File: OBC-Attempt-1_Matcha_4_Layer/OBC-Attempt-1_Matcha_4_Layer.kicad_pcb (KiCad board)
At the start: 4 copper layers, 75 parts, among them J1 Screw_Terminal_01x08, J2 Screw_Terminal_01x08, J3 USB_B_Micro, J4 Screw_Terminal_01x08, J5 Conn_01x04, J6 Micro_SD_Card, J7 Screw_Terminal_01x02, J8 Screw_Terminal_01x02, Q1 2N7002K, Q2 2N7002K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

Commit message: Some 4 Layer Work :)
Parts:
- removed C14: 26pf, Capacitor_SMD:C_01005_0402Metric
- removed C18: 26uf, Capacitor_SMD:C_01005_0402Metric
- removed Y2: ABMM2-32.768MHZ-E2F-T, ABMM2_6mm_3_6mm:XTAL_ABMM2-32.768MHZ-E2F-T
- added H1: MountingHole_Pad, MountingHole:MountingHole_3mm_Pad_TopBottom, F.Cu at (76.2, 31.8)
- added H2: MountingHole_Pad, MountingHole:MountingHole_3mm_Pad_TopBottom, F.Cu at (31.8, 31.8)
- added H3: MountingHole_Pad, MountingHole:MountingHole_3mm_Pad_TopBottom, F.Cu at (31.8, 76.2)
- added H4: MountingHole_Pad, MountingHole:MountingHole_3mm_Pad_TopBottom, F.Cu at (76.2, 76.2)
- BZ1, J5, Q1, Q2, Q3, Q4, R10, R11, R12, R14, R15, R16, R17, R9, U10, U11, U2, U3, U4, U5, U7, U8: moved to B.Cu
- C1, C10, C11, C13, C15, C16, C17, C2, C3, C4, C6, C7, C8, C9: footprint Capacitor_SMD:C_01005_0402Metric -> Capacitor_SMD:C_0402_1005Metric
- C12, C5: footprint Capacitor_SMD:C_0201_0603Metric -> Capacitor_SMD:C_0603_1608Metric; moved to F.Cu
- C20, C21: footprint Capacitor_SMD:C_0201_0603Metric -> Capacitor_SMD:C_0603_1608Metric
- D1, D2, D3, D4, D5, D6, D7, D8: footprint Diode_SMD:D_SMC -> Diode_SMD:D_SMA; moved to B.Cu
- J1, J2, J4: footprint TerminalBlock_Phoenix:TerminalBlock_Phoenix_MKDS-1,5-8_1x08_P5.00mm_Horizontal -> TerminalBlock_Phoenix:TerminalBlock_Phoenix_MPT-0,5-8-2.54_1x08_P2.54mm_Horizontal
- J3, U6: moved to F.Cu
- J7, J8: footprint TerminalBlock_Phoenix:TerminalBlock_Phoenix_MKDS-1,5-2_1x02_P5.00mm_Horizontal -> TerminalBlock_Phoenix:TerminalBlock_Phoenix_MPT-0,5-2-2.54_1x02_P2.54mm_Horizontal; moved to B.Cu
- R1, R2, R3, R4, R5, R6, R7, R8: footprint Resistor_SMD:R_0201_0603Metric -> Resistor_SMD:R_0603_1608Metric; moved to B.Cu
- R13: footprint Resistor_SMD:R_01005_0402Metric -> Resistor_SMD:R_0603_1608Metric
- R18, R19: footprint Resistor_SMD:R_0201_0603Metric -> Resistor_SMD:R_0603_1608Metric
- moved J3 139.4 mm to (40.7, 28.3), turned to 180 degrees
- moved J7 135.2 mm to (40.5, 78.8)
- moved J8 133.2 mm to (47.4, 78.8), turned to 180 degrees
- moved C5 131.9 mm to (42.8, 32.0)
- moved C12 125.3 mm to (46.1, 42.6), turned to 0 degrees
- moved R18 124.0 mm to (50.0, 72.5), turned to 90 degrees
- moved C20 123.5 mm to (48.0, 72.5), turned to 90 degrees
- moved U6 122.9 mm to (44.0, 37.3), turned to -90 degrees
- moved U12 120.7 mm to (43.5, 70.6), turned to 90 degrees
- moved R19 120.3 mm to (50.0, 69.4), turned to 90 degrees
- moved C21 112.2 mm to (44.6, 63.2), turned to 180 degrees
- moved J6 106.0 mm to (63.7, 74.0), turned to 0 degrees
- moved U1 94.2 mm to (55.7, 51.5), turned to 135 degrees
- moved C7 89.1 mm to (55.8, 45.9), turned to 180 degrees
- moved C9 88.8 mm to (57.2, 46.8), turned to 90 degrees
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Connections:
- C20 pad 1: PWR -> BATT+
- R18 pad 1: PWR -> unconnected-(R18-Pad1)
- U12 pad 3: PWR -> BATT+
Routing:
- net GND: track 174.6 -> 0.00 mm, vias 5 -> 0
- net PWR: track 87.8 -> 0.00 mm
- net 3.3V: track 39.3 -> 0.00 mm, vias 4 -> 0
- net USB_OTG_FS_ID: track 35.0 -> 0.00 mm, vias 1 -> 0
- net SDIO_CMD: track 34.0 -> 0.00 mm
- net VMON: track 33.4 -> 0.00 mm
- net USB_OTG_FS_DP: track 32.4 -> 0.00 mm, vias 1 -> 0
- net SDIO_D3: track 30.3 -> 0.00 mm
- net SDIO_D0: track 29.8 -> 0.00 mm
- net SDIO_CK: track 26.7 -> 0.00 mm
- net USB_OTG_FS_DM: track 25.7 -> 0.00 mm, vias 1 -> 0
- net SDIO_D1: track 25.6 -> 0.00 mm
- net SDIO_D2: track 24.2 -> 0.00 mm
- net BATT+: track 17.3 -> 0.00 mm
- net RCC_OSC_IN: track 11.9 -> 0.00 mm
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- added copper zone on In2.Cu, net 3.3V
- added copper zone on In1.Cu, net GND
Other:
- board outline added: 57.1 x 57.1 mm

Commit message: start over
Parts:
- moved C5 175.9 mm to (200.2, 110.4)
- moved C12 175.9 mm to (203.6, 121.0)
- moved J3 175.9 mm to (198.2, 106.7)
- moved U6 175.9 mm to (201.4, 115.7)
- moved D4 158.3 mm to (189.0, 25.9)
- moved R11 158.3 mm to (199.9, 38.0)
- moved R9 158.3 mm to (199.7, 31.0)
- moved U4 158.3 mm to (194.6, 39.3)
- moved D1 158.3 mm to (189.0, 40.1)
- moved D2 158.3 mm to (189.0, 18.7)
- moved D3 158.3 mm to (189.0, 33.0)
- moved J2 158.3 mm to (185.6, 38.7)
- moved R10 158.3 mm to (199.7, 23.9)
- moved R12 158.3 mm to (199.6, 16.7)
- moved U2 158.3 mm to (194.4, 32.3)
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
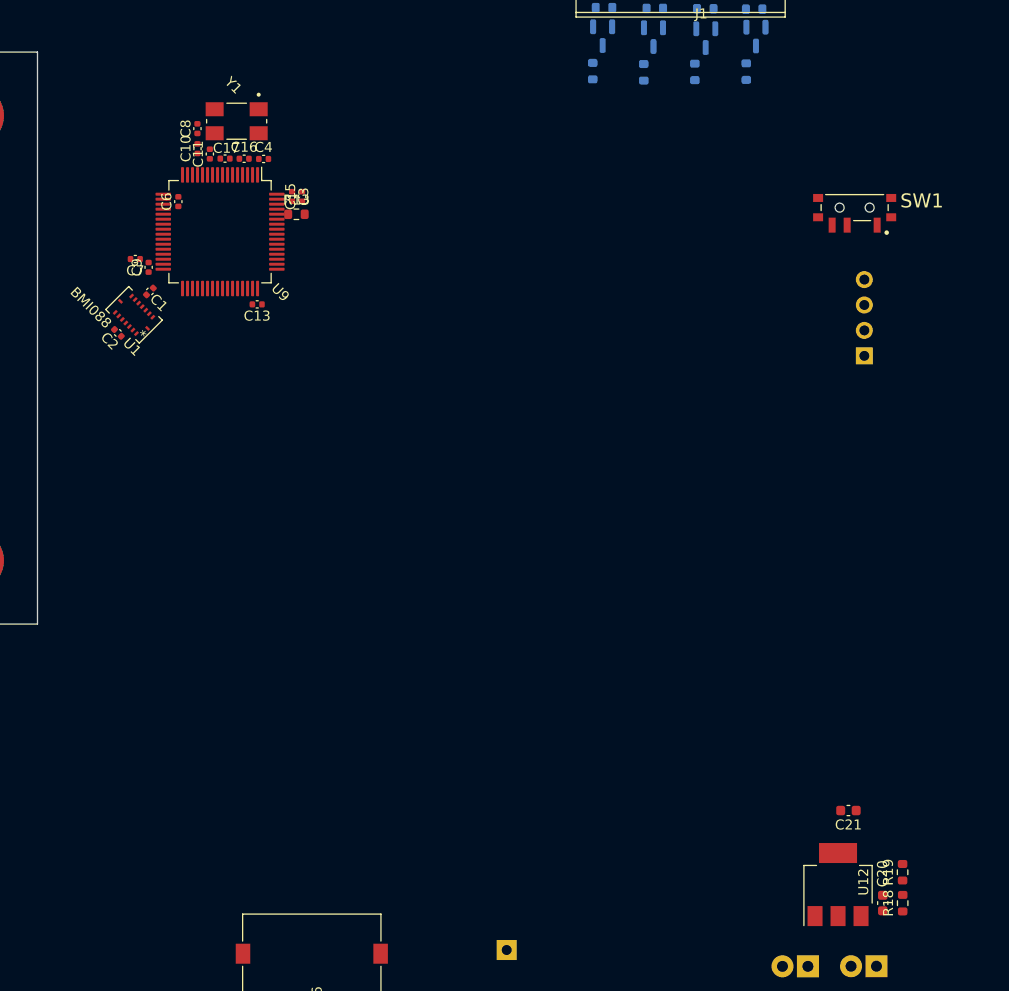
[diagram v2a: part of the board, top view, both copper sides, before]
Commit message: reorg mpu
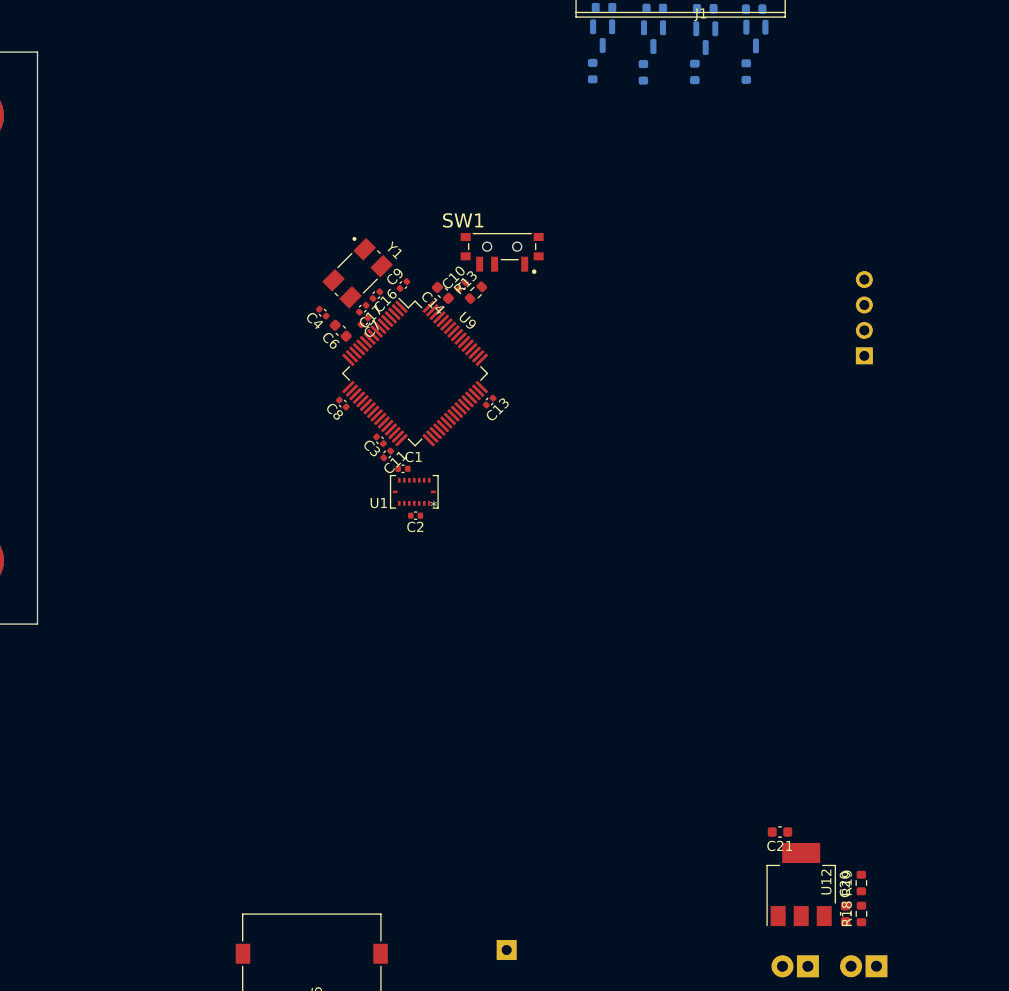
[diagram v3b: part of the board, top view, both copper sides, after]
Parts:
- removed C15: 4.7uF, Capacitor_SMD:C_0402_1005Metric
- added C14: 4.7uF, Capacitor_SMD:C_0603_1608Metric, F.Cu at (123.1, 49.5)
- C10: value 1uF -> 100nF
- C3: value 100nF -> 4.7uF
- C6: value 100nF -> 1uF; footprint Capacitor_SMD:C_0402_1005Metric -> Capacitor_SMD:C_0603_1608Metric
- C7: value 4.7uF -> 100nF
- moved SW1 35.4 mm to (129.0, 44.8)
- moved C2 34.9 mm to (120.3, 71.7), turned to 180 degrees
- moved C11 34.9 mm to (117.5, 65.6), turned to -135 degrees
- moved U1 33.1 mm to (120.2, 69.3), turned to 180 degrees
- moved C8 31.1 mm to (113.1, 60.5), turned to 135 degrees
- moved C1 30.9 mm to (119.1, 67.0), turned to 180 degrees
- moved C10 29.8 mm to (125.0, 48.8), turned to 45 degrees
- moved C3 25.9 mm to (116.8, 64.2), turned to 135 degrees
- moved C9 25.5 mm to (119.1, 48.7), turned to 45 degrees
- moved C13 25.2 mm to (127.7, 60.3), turned to -135 degrees
- moved U9 24.1 mm to (120.3, 57.5), turned to -45 degrees
- moved C7 23.7 mm to (115.2, 52.3), turned to -135 degrees
- moved C6 20.7 mm to (112.8, 53.2), turned to 135 degrees
- moved C17 20.4 mm to (115.0, 51.0), turned to -135 degrees
- moved R13 19.6 mm to (126.4, 49.4), turned to 45 degrees
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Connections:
- C10 pad 2: Net-(C10-Pad2) -> GND
- C11 pad 1: Net-(C11-Pad1) -> 3.3V
- C3 pad 1: 3.3V -> Net-(C3-Pad1)
- C4 pad 1: 3.3V -> Net-(C4-Pad1)
- C6 pad 2: GND -> Net-(C4-Pad1)
- C8 pad 1: Net-(C10-Pad2) -> 3.3V
- R18 pad 1: unconnected-(R18-Pad1) -> BATT+
- SW1 pad S2: unconnected-(SW1-PadS1) -> unconnected-(SW1-PadS2)
- SW1 pad S3: unconnected-(SW1-PadS1) -> unconnected-(SW1-PadS3)
- SW1 pad S4: unconnected-(SW1-PadS1) -> unconnected-(SW1-PadS4)
- U9 pad 11: PYRO1 -> PYRO4
- U9 pad 14: PYRO2 -> PYRO3
- U9 pad 15: PYRO3 -> PYRO1
- U9 pad 16: PYRO4 -> PYRO2
- U9 pad 20: unconnected-(U9-Pad20) -> CS2_GYRO
- U9 pad 24: CS2_GYRO -> SOL2
- U9 pad 25: CS1_ACC -> SOL3
- U9 pad 27: SOL2 -> SOL4
- U9 pad 28: SOL3 -> SOL5
- U9 pad 29: SOL4 -> unconnected-(U9-Pad29)
- U9 pad 30: Net-(C7-Pad1) -> Net-(C3-Pad1)
- U9 pad 33: SOL5 -> INT_GYRO1
- U9 pad 34: SOL6 -> INT_GYRO2
- U9 pad 35: SOL7 -> CS1_ACC
- U9 pad 36: SOL8 -> INT_ACC1
- U9 pad 37: INT_ACC1 -> INT_ACC2
- U9 pad 38: INT_ACC2 -> SOL6
- U9 pad 41: INT_GYRO1 -> SOL7
- U9 pad 42: INT_GYRO2 -> SOL8
- U9 pad 7: Net-(C11-Pad1) -> Net-(C7-Pad1)

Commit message: Cant move stuff
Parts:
- moved R15 0.56 mm to (206.1, 41.0)
- moved U1 0.06 mm to (120.2, 69.4)
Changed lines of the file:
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@@
   )
   (footprint "BMI088:BMI088" (layer "F.Cu")
-    (at 120.2 69.34 180)
+    (at 120.19 69.4 180)
     (property "AVAILABILITY" "In Stock")
     (property "DESCRIPTION" "Accelerometer, Gyroscope, 6 Axis Sensor I²C, SPI Output")
@@
   )
   (footprint "Resistor_SMD:R_0603_1608Metric" (layer "B.Cu")
-    (at 206.665 41.01 180)
+    (at 206.11 41.05 180)
     (descr "Resistor SMD 0603 (1608 Metric), square (rectangular) end terminal, IPC_7351 nominal, (Body size source: IPC-SM-782 page 72, https://www.pcb-3d.com/wordpress/wp-content/uploads/ipc-sm-782a_amendment_1_and_2.pdf), generated with kicad-footprint-generator")
     (tags "resistor")
